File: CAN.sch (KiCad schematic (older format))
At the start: 12 parts, among them J5 DB9_Male, U1 LPC54616J512, U5 TJA1051T

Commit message: Fix few bugs, review design
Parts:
- added R11: NC, Resistor_SMD:R_0805_2012Metric_Pad1.15x1.40mm_HandSolder, symbol canbox-rescue:R-Device
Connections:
- net +5V: now also R11.1
- net CAN_H: now also J5.7; no longer J5.8
- net CAN_L: now also J5.2; no longer J5.1
- net at U5.5 (NC_EN): now also R11.2
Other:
- note added: "->"
- note added: "<-"
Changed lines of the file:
@@
 encoding utf-8
 Sheet 4 6
-Title ""
-Date ""
-Rev ""
-Comp ""
+Title "CANBOX LPC546xx - CAN"
+Date "2019-06-02"
+Rev "1"
+Comp "Thorsten Wilmer"
 Comment1 ""
 Comment2 ""
@@
 $EndComp
 Wire Wire Line
-	6350 2050 6350 1600
+	6350 2050 6350 1700
 Text HLabel 850  1500 0    50   Input ~ 0
 5V
@@
 $EndComp
 Wire Wire Line
-	10400 3350 9950 3350
-Wire Wire Line
-	9950 3350 9950 2750
-Wire Wire Line
-	10400 3850 10150 3850
-Wire Wire Line
-	10150 3850 10150 2550
-Wire Wire Line
 	8200 2550 9200 2550
 Wire Wire Line
@@
 	3850 2350 5850 2350
 Wire Wire Line
-	5850 2650 5750 2650
-Wire Wire Line
-	5750 2650 5750 2450
-Wire Wire Line
-	3850 2450 5750 2450
+	5850 2650 5300 2650
+Wire Wire Line
+	5300 2650 5300 2450
+Wire Wire Line
+	3850 2450 5300 2450
 Wire Wire Line
 	6350 2850 6350 3000
@@
 Wire Wire Line
 	9200 2550 10150 2550
-NoConn ~ 10400 3550
-NoConn ~ 10400 3650
 NoConn ~ 3850 2900
 NoConn ~ 3850 2800
 NoConn ~ 3850 2700
+$Comp
+L canbox-rescue:R-Device R11
+U 1 1 5CFFAE5F
+P 5450 1950
+F 0 "R11" H 5520 1996 50  0000 L CNN
+F 1 "NC" H 5520 1905 50  0000 L CNN
+F 2 "Resistor_SMD:R_0805_2012Metric_Pad1.15x1.40mm_HandSolder" V 5380 1950 50  0001 C CNN
+F 3 "" H 5450 1950 50  0001 C CNN
+	1    5450 1950
+	1    0    0    -1
+$EndComp
+Wire Wire Line
+	5850 2550 5450 2550
+Wire Wire Line
+	5450 2550 5450 2100
+Wire Wire Line
+	5450 1800 5450 1700
+Wire Wire Line
+	5450 1700 6350 1700
+Connection ~ 6350 1700
+Wire Wire Line
+	6350 1700 6350 1600
+Wire Wire Line
+	10400 3550 9950 3550
+Wire Wire Line
+	9950 2750 9950 3550
+NoConn ~ 10400 3350
+Wire Wire Line
+	10400 3650 10150 3650
+Wire Wire Line
+	10150 3650 10150 2550
+NoConn ~ 10400 3850
+Text Notes 5600 2400 0    50   ~ 0
+<-
+Text Notes 5650 2250 0    50   ~ 0
+->
 $EndSCHEMATC

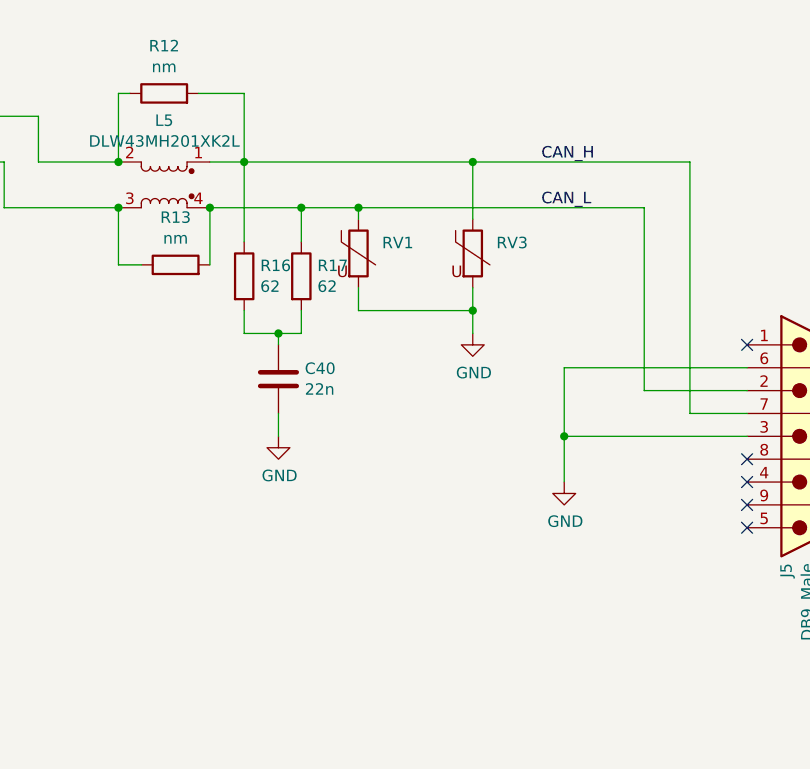
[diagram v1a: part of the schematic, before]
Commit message: Add solder jumper for termination.
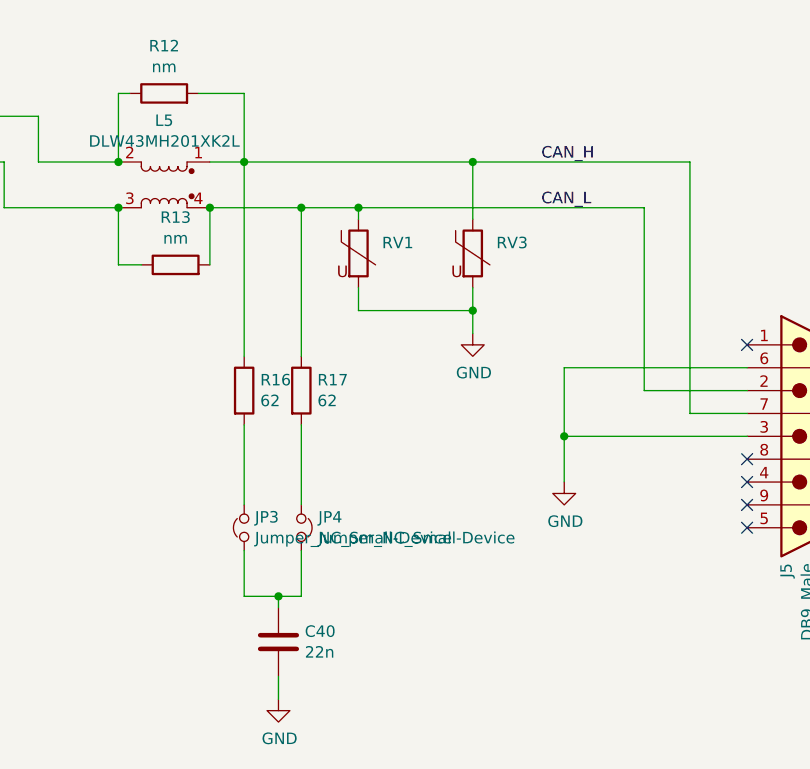
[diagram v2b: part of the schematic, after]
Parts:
- added JP3, JP4: Jumper_NC_Small-Device, Jumper:SolderJumper-2_P1.3mm_Open_Pad1.0x1.5mm, symbol canbox-rescue:Jumper_NC_Small-Device
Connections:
- new net: JP3.2, R16.2
- new net: JP4.1, R17.2
- new net: C40.1, JP3.1, JP4.2
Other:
- moved on the sheet: C40, R16, R17
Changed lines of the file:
@@
 Wire Wire Line
 	8700 2800 8700 2750
-Wire Wire Line
-	8050 2750 8450 2750
 Connection ~ 8700 2750
 $Comp
@@
 L canbox-rescue:R-Device R16
 U 1 1 5C3B1DC6
-P 8200 3050
-F 0 "R16" H 8270 3096 50  0000 L CNN
-F 1 "62" H 8270 3005 50  0000 L CNN
-F 2 "Resistor_SMD:R_0805_2012Metric_Pad1.15x1.40mm_HandSolder" V 8130 3050 50  0001 C CNN
-F 3 "~" H 8200 3050 50  0001 C CNN
-F 4 "ERJ-6ENF59R0V" H 400 -350 50  0001 C CNN "OP"
-F 5 "ok" H 0   0   50  0001 C CNN "Mouser"
-F 6 "ok" H 0   0   50  0001 C CNN "notes"
-	1    8200 3050
+P 8200 3550
+F 0 "R16" H 8270 3596 50  0000 L CNN
+F 1 "62" H 8270 3505 50  0000 L CNN
+F 2 "Resistor_SMD:R_0805_2012Metric_Pad1.15x1.40mm_HandSolder" V 8130 3550 50  0001 C CNN
+F 3 "~" H 8200 3550 50  0001 C CNN
+F 4 "ERJ-6ENF59R0V" H 400 150 50  0001 C CNN "OP"
+F 5 "ok" H 0   500 50  0001 C CNN "Mouser"
+F 6 "ok" H 0   500 50  0001 C CNN "notes"
+	1    8200 3550
 	1    0    0    -1
 $EndComp
@@
 L canbox-rescue:R-Device R17
 U 1 1 5C3B4F36
-P 8450 3050
-F 0 "R17" H 8520 3096 50  0000 L CNN
-F 1 "62" H 8520 3005 50  0000 L CNN
-F 2 "Resistor_SMD:R_0805_2012Metric_Pad1.15x1.40mm_HandSolder" V 8380 3050 50  0001 C CNN
-F 3 "~" H 8450 3050 50  0001 C CNN
-F 4 "ERJ-6ENF59R0V" H 400 -350 50  0001 C CNN "OP"
-F 5 "ok" H 0   0   50  0001 C CNN "Mouser"
-F 6 "ok" H 0   0   50  0001 C CNN "notes"
-	1    8450 3050
+P 8450 3550
+F 0 "R17" H 8520 3596 50  0000 L CNN
+F 1 "62" H 8520 3505 50  0000 L CNN
+F 2 "Resistor_SMD:R_0805_2012Metric_Pad1.15x1.40mm_HandSolder" V 8380 3550 50  0001 C CNN
+F 3 "~" H 8450 3550 50  0001 C CNN
+F 4 "ERJ-6ENF59R0V" H 400 150 50  0001 C CNN "OP"
+F 5 "ok" H 0   500 50  0001 C CNN "Mouser"
+F 6 "ok" H 0   500 50  0001 C CNN "notes"
+	1    8450 3550
 	1    0    0    -1
 $EndComp
@@
 L canbox-rescue:C-Device C40
 U 1 1 5C3C3F1C
-P 8350 3500
-F 0 "C40" H 8465 3546 50  0000 L CNN
-F 1 "22n" H 8465 3455 50  0000 L CNN
-F 2 "Capacitor_SMD:C_0805_2012Metric_Pad1.15x1.40mm_HandSolder" H 8388 3350 50  0001 C CNN
-F 3 "~" H 8350 3500 50  0001 C CNN
-F 4 "C0805C223K5RACTU" H 400 -350 50  0001 C CNN "OP"
-F 5 "ali" H 0   0   50  0001 C CNN "notes"
-	1    8350 3500
-	1    0    0    -1
-$EndComp
-Wire Wire Line
-	8200 2900 8200 2550
+P 8350 4650
+F 0 "C40" H 8465 4696 50  0000 L CNN
+F 1 "22n" H 8465 4605 50  0000 L CNN
+F 2 "Capacitor_SMD:C_0805_2012Metric_Pad1.15x1.40mm_HandSolder" H 8388 4500 50  0001 C CNN
+F 3 "~" H 8350 4650 50  0001 C CNN
+F 4 "C0805C223K5RACTU" H 400 800 50  0001 C CNN "OP"
+F 5 "ali" H 0   1150 50  0001 C CNN "notes"
+	1    8350 4650
+	1    0    0    -1
+$EndComp
 Connection ~ 8200 2550
 Wire Wire Line
-	8450 2900 8450 2750
-Connection ~ 8450 2750
-Wire Wire Line
-	8450 2750 8700 2750
-Wire Wire Line
-	8200 3200 8200 3300
-Wire Wire Line
-	8200 3300 8350 3300
-Wire Wire Line
-	8450 3300 8450 3200
-Wire Wire Line
-	8350 3350 8350 3300
-Connection ~ 8350 3300
-Wire Wire Line
-	8350 3300 8450 3300
-Wire Wire Line
-	8350 3750 8350 3650
+	8200 4250 8200 4450
+Wire Wire Line
+	8200 4450 8350 4450
+Wire Wire Line
+	8450 4450 8450 4250
+Wire Wire Line
+	8350 4500 8350 4450
+Connection ~ 8350 4450
+Wire Wire Line
+	8350 4450 8450 4450
+Wire Wire Line
+	8350 4900 8350 4800
 Wire Wire Line
 	8050 3000 8050 2750
@@
 L canbox-rescue:GND-power #PWR0105
 U 1 1 5C0835E8
-P 8350 3750
-F 0 "#PWR0105" H 8350 3500 50  0001 C CNN
-F 1 "GND" H 8355 3577 50  0000 C CNN
-F 2 "" H 8350 3750 50  0001 C CNN
-F 3 "" H 8350 3750 50  0001 C CNN
-	1    8350 3750
+P 8350 4900
+F 0 "#PWR0105" H 8350 4650 50  0001 C CNN
+F 1 "GND" H 8355 4727 50  0000 C CNN
+F 2 "" H 8350 4900 50  0001 C CNN
+F 3 "" H 8350 4900 50  0001 C CNN
+	1    8350 4900
 	1    0    0    -1
 $EndComp
@@
 Text Notes 5650 2250 0    50   ~ 0
 ->
+$Comp
+L canbox-rescue:Jumper_NC_Small-Device JP4
+U 1 1 5D07D244
+P 8450 4150
+F 0 "JP4" V 8404 4224 50  0000 L CNN
+F 1 "Jumper_NC_Small-Device" V 8495 4224 50  0000 L CNN
+F 2 "Jumper:SolderJumper-2_P1.3mm_Open_Pad1.0x1.5mm" H 8450 4150 50  0001 C CNN
+F 3 "" H 8450 4150 50  0001 C CNN
+	1    8450 4150
+	0    1    1    0
+$EndComp
+$Comp
+L canbox-rescue:Jumper_NC_Small-Device JP3
+U 1 1 5D07E798
+P 8200 4150
+AR Path="/5BDA19BB/5D07E798" Ref="JP3"  Part="1"
+AR Path="/5BD9E863/5D07E798" Ref="JP3"  Part="1"
+F 0 "JP3" V 8246 4103 50  0000 R CNN
+F 1 "Jumper_NC_Small-Device" V 8155 4103 50  0000 R CNN
+F 2 "Jumper:SolderJumper-2_P1.3mm_Open_Pad1.0x1.5mm" H 8200 4150 50  0001 C CNN
+F 3 "" H 8200 4150 50  0001 C CNN
+	1    8200 4150
+	0    -1   -1   0
+$EndComp
+Wire Wire Line
+	8050 2750 8450 2750
+Wire Wire Line
+	8450 2750 8450 3400
+Connection ~ 8450 2750
+Wire Wire Line
+	8450 2750 8700 2750
+Wire Wire Line
+	8200 3400 8200 2550
+Wire Wire Line
+	8200 3700 8200 4050
+Wire Wire Line
+	8450 3700 8450 4050
 $EndSCHEMATC

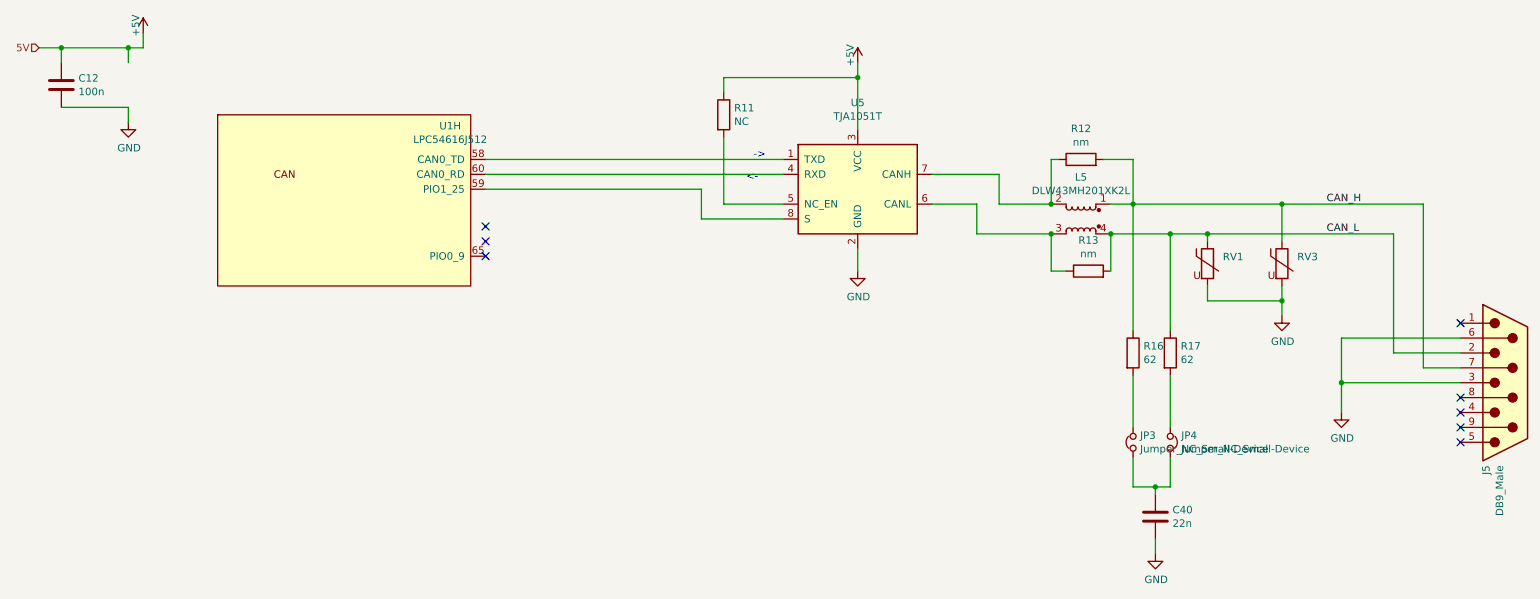
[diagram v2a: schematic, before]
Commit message: V3 bigger board, RMII instrumentation, inverter
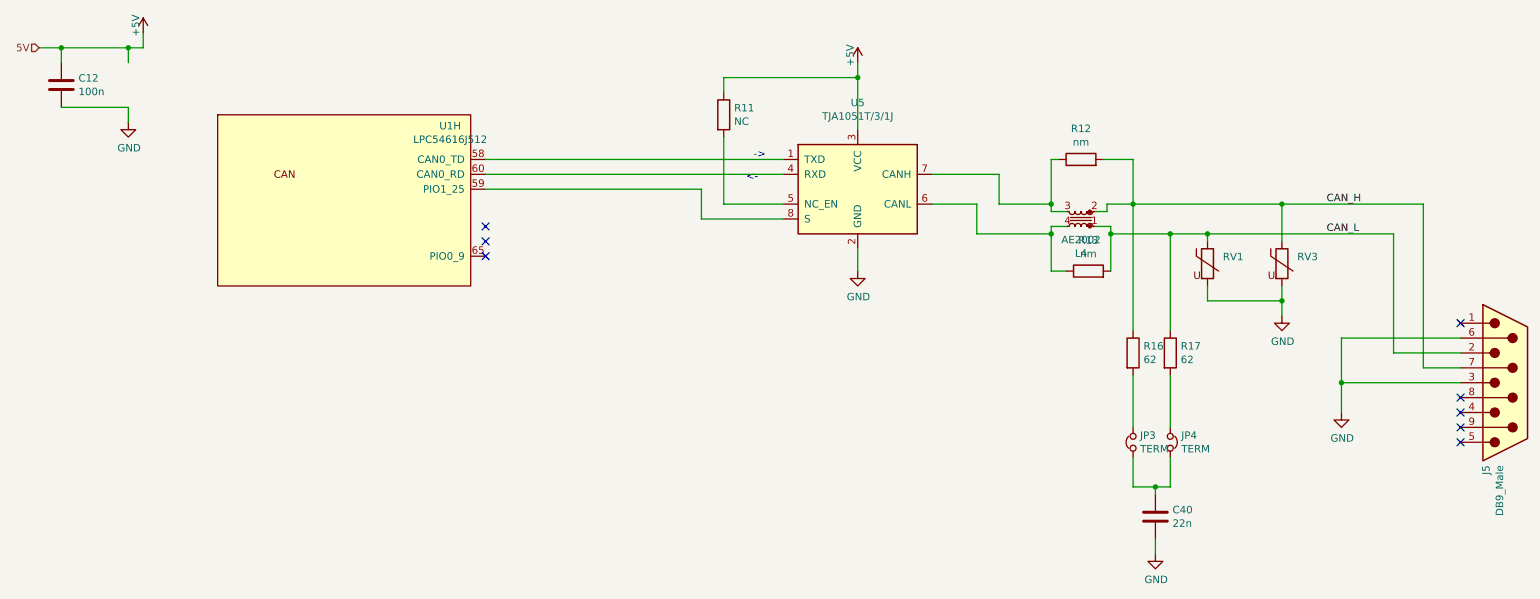
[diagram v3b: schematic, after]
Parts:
- removed L5: DLW43MH201XK2L, cypress:DLW43MH201XK2L, symbol canbox-rescue:DLW43MH201XK2L-cypress
- added L4: AE2002, Inductor_SMD:L_CMC_1812, symbol canbox-rescue:L_Core_Iron_Coupled_Small-Device
- C12: JLC (none) -> C49678; OP C0805C103K1RACTU -> CC0805KRX7R9BB104
- C40: JLC (none) -> C1729
- JP3, JP4: value Jumper_NC_Small-Device -> TERM
- R16, R17: JLC (none) -> C17767; OP ERJ-6ENF59R0V -> 0805W8F6201T5E
- U5: value TJA1051T -> TJA1051T/3/1J; JLC (none) -> C38695
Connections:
- net CAN_H: now also L4.2
- net CAN_L: now also L4.1
- net at R13.1, U5.6 (CANL): now also L4.4
- net at R12.1, U5.7 (CANH): now also L4.3
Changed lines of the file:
@@
-EESchema Schematic File Version 4
+EESchema Schematic File Version 5
 LIBS:canbox-cache
-EELAYER 29 0
+EELAYER 30 0
 EELAYER END
 $Descr A4 11693 8268
@@
 Comment3 ""
 Comment4 ""
+Comment5 ""
+Comment6 ""
+Comment7 ""
+Comment8 ""
+Comment9 ""
 $EndDescr
 $Comp
@@
 	1    9200 2950
 	1    0    0    -1
-$EndComp
-$Comp
-L canbox-rescue:DLW43MH201XK2L-cypress L5
-U 1 1 5C690F7D
-P 7850 2650
-F 0 "L5" H 7850 2931 50  0000 C CNN
-F 1 "DLW43MH201XK2L" H 7850 2840 50  0000 C CNN
-F 2 "cypress:DLW43MH201XK2L" H 7850 2650 50  0001 C CNN
-F 3 "~" H 7850 2650 50  0001 C CNN
-F 4 "DLW43MH201XK2L" H 400 -350 50  0001 C CNN "OP"
-F 5 "DLW43MH201XK2L" H 0   0   50  0001 C CNN "Arrow"
-F 6 "490-14325-1-ND  " H 0   0   50  0001 C CNN "DigiKez"
-	1    7850 2650
-	-1   0    0    -1
 $EndComp
 $Comp
@@
 $EndComp
 Wire Wire Line
-	8200 2550 8050 2550
-Wire Wire Line
 	8700 2800 8700 2750
 Connection ~ 8700 2750
@@
 F 2 "Resistor_SMD:R_0805_2012Metric_Pad1.15x1.40mm_HandSolder" V 8130 3550 50  0001 C CNN
 F 3 "~" H 8200 3550 50  0001 C CNN
-F 4 "ERJ-6ENF59R0V" H 400 150 50  0001 C CNN "OP"
+F 4 "0805W8F6201T5E" H 400 150 50  0001 C CNN "OP"
 F 5 "ok" H 0   500 50  0001 C CNN "Mouser"
 F 6 "ok" H 0   500 50  0001 C CNN "notes"
+F 7 "C17767" H 8200 3550 50  0001 C CNN "JLC"
 	1    8200 3550
 	1    0    0    -1
@@
 F 2 "Resistor_SMD:R_0805_2012Metric_Pad1.15x1.40mm_HandSolder" V 8380 3550 50  0001 C CNN
 F 3 "~" H 8450 3550 50  0001 C CNN
-F 4 "ERJ-6ENF59R0V" H 400 150 50  0001 C CNN "OP"
+F 4 "0805W8F6201T5E" H 400 150 50  0001 C CNN "OP"
 F 5 "ok" H 0   500 50  0001 C CNN "Mouser"
 F 6 "ok" H 0   500 50  0001 C CNN "notes"
+F 7 "C17767" H 8450 3550 50  0001 C CNN "JLC"
 	1    8450 3550
 	1    0    0    -1
@@
 F 4 "C0805C223K5RACTU" H 400 800 50  0001 C CNN "OP"
 F 5 "ali" H 0   1150 50  0001 C CNN "notes"
+F 6 "C1729 " H 8350 4650 50  0001 C CNN "JLC"
 	1    8350 4650
 	1    0    0    -1
@@
 Wire Wire Line
 	8050 3000 8050 2750
-Connection ~ 8050 2750
 Wire Wire Line
 	7650 3000 7650 2750
 Wire Wire Line
 	7650 3000 7750 3000
-Connection ~ 7650 2750
 Wire Wire Line
 	7650 2550 7650 2250
 Wire Wire Line
 	7650 2250 7700 2250
-Connection ~ 7650 2550
 Wire Wire Line
 	8000 2250 8200 2250
@@
 P 6350 2450
 F 0 "U5" H 6350 3031 50  0000 C CNN
-F 1 "TJA1051T" H 6350 2940 50  0000 C CNN
+F 1 "TJA1051T/3/1J" H 6350 2940 50  0000 C CNN
 F 2 "Package_SO:SOIC-8_3.9x4.9mm_P1.27mm" H 6350 1950 50  0001 C CIN
 F 3 "http://www.nxp.com/documents/data_sheet/TJA1051.pdf" H 6350 2450 50  0001 C CNN
 F 4 "ali" H 0   0   50  0001 C CNN "notes"
+F 5 "C38695" H 6350 2450 50  0001 C CNN "JLC"
 	1    6350 2450
 	1    0    0    -1
@@
 F 2 "Capacitor_SMD:C_0805_2012Metric_Pad1.15x1.40mm_HandSolder" H 1038 1600 50  0001 C CNN
 F 3 "~" H 1000 1750 50  0001 C CNN
-F 4 "C0805C103K1RACTU" H -450 0   50  0001 C CNN "OP"
+F 4 "CC0805KRX7R9BB104" H -450 0   50  0001 C CNN "OP"
 F 5 "ali" H 0   0   50  0001 C CNN "notes"
+F 6 " C49678 " H 1000 1750 50  0001 C CNN "JLC"
 	1    1000 1750
 	1    0    0    -1
@@
 P 8450 4150
 F 0 "JP4" V 8404 4224 50  0000 L CNN
-F 1 "Jumper_NC_Small-Device" V 8495 4224 50  0000 L CNN
+F 1 "TERM" V 8495 4224 50  0000 L CNN
 F 2 "Jumper:SolderJumper-2_P1.3mm_Open_Pad1.0x1.5mm" H 8450 4150 50  0001 C CNN
 F 3 "" H 8450 4150 50  0001 C CNN
@@
 $Comp
 L canbox-rescue:Jumper_NC_Small-Device JP3
-U 1 1 5D07E798
+U 1 1 5DA2AD5D
 P 8200 4150
-AR Path="/5BDA19BB/5D07E798" Ref="JP3"  Part="1"
-AR Path="/5BD9E863/5D07E798" Ref="JP3"  Part="1"
+AR Path="/5BDA19BB/5DA2AD5D" Ref="JP3"  Part="1"
+AR Path="/5BD9E863/5DA2AD5D" Ref="JP3"  Part="1"
 F 0 "JP3" V 8246 4103 50  0000 R CNN
-F 1 "Jumper_NC_Small-Device" V 8155 4103 50  0000 R CNN
+F 1 "TERM" V 8155 4103 50  0000 R CNN
 F 2 "Jumper:SolderJumper-2_P1.3mm_Open_Pad1.0x1.5mm" H 8200 4150 50  0001 C CNN
 F 3 "" H 8200 4150 50  0001 C CNN
@@
 Wire Wire Line
 	8450 3700 8450 4050
+$Comp
+L canbox-rescue:L_Core_Iron_Coupled_Small-Device L4
+U 1 1 5E74A7ED
+P 7850 2650
+F 0 "L4" H 7850 2881 50  0000 C CNN
+F 1 "AE2002" H 7850 2790 50  0000 C CNN
+F 2 "Inductor_SMD:L_CMC_1812" H 7850 2650 50  0001 C CNN
+F 3 "~" H 7850 2650 50  0001 C CNN
+F 4 "1840-1044-1-ND" H -1750 -1150 50  0001 C CNN "OP"
+F 5 "AE2002" H -1750 -1150 50  0001 C CNN "Arrow"
+F 6 "1840-1044-1-ND" H -1750 -1150 50  0001 C CNN "DigiKez"
+	1    7850 2650
+	-1   0    0    1
+$EndComp
+Wire Wire Line
+	7950 2600 8025 2600
+Wire Wire Line
+	8025 2600 8025 2550
+Wire Wire Line
+	8025 2550 8200 2550
+Wire Wire Line
+	7950 2700 8050 2700
+Wire Wire Line
+	8050 2700 8050 2750
+Connection ~ 8050 2750
+Wire Wire Line
+	7750 2700 7650 2700
+Wire Wire Line
+	7650 2700 7650 2750
+Connection ~ 7650 2750
+Wire Wire Line
+	7750 2600 7650 2600
+Wire Wire Line
+	7650 2600 7650 2550
+Connection ~ 7650 2550
 $EndSCHEMATC

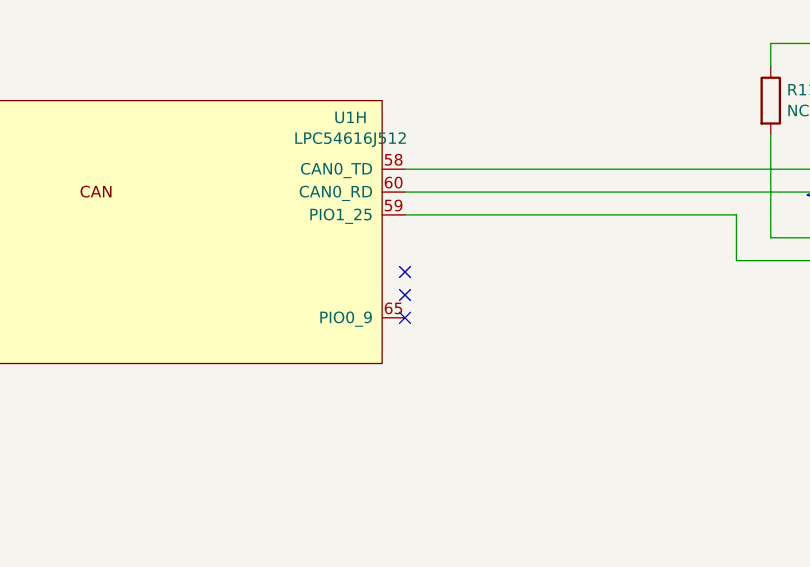
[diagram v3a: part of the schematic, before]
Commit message: V5 now impedance controlled
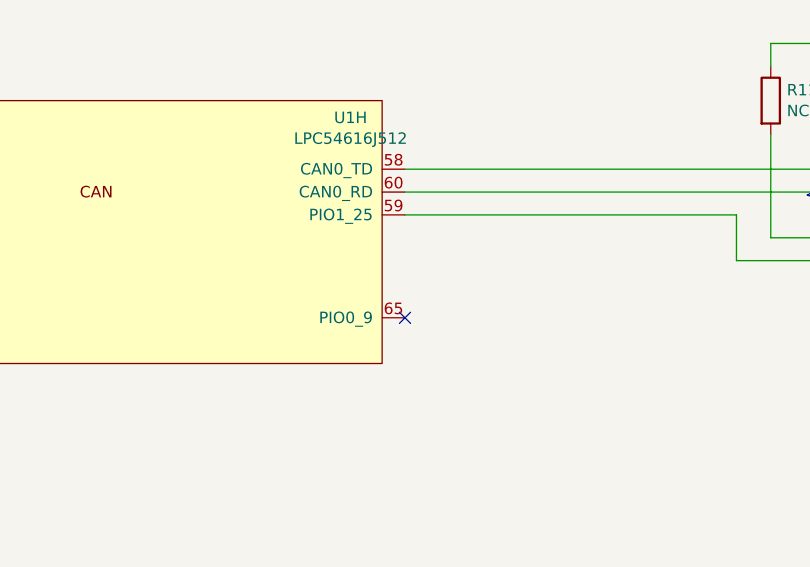
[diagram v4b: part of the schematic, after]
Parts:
- L4: footprint Inductor_SMD:L_CMC_1812 -> cypress:L_CMC_1812
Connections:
- no-connect marks 8 -> 6
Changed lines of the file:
@@
 	9200 2550 10150 2550
 NoConn ~ 3850 2900
-NoConn ~ 3850 2800
-NoConn ~ 3850 2700
 $Comp
 L canbox-rescue:R-Device R11
@@
 F 0 "L4" H 7850 2881 50  0000 C CNN
 F 1 "AE2002" H 7850 2790 50  0000 C CNN
-F 2 "Inductor_SMD:L_CMC_1812" H 7850 2650 50  0001 C CNN
+F 2 "cypress:L_CMC_1812" H 7850 2650 50  0001 C CNN
 F 3 "~" H 7850 2650 50  0001 C CNN
 F 4 "1840-1044-1-ND" H -1750 -1150 50  0001 C CNN "OP"
